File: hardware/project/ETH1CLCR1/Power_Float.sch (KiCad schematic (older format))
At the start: 56 parts, among them U602 LM1117IMP-3.3/NOPB, U604 LM1117IMP-3.3/NOPB, U608 LM1117IMP-5.0/NOPB, U609 TSR1-2490, U701 THL15-2415WI, U703 MC7815BD2TG, U705 TSR2-2450, U706 LT8330_S6, U707 MC7915BD2TG, U710 LT8330_S6

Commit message: Schematic design
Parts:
- removed U703: MC7815BD2TG, Package_TO_SOT_SMD:TO-263-2, symbol Regulator_Linear:L7815
- removed U707: MC7915BD2TG, Package_TO_SOT_SMD:TO-263-2, symbol Regulator_Linear:L7915
- added U?: L7815, symbol Regulator_Linear:L7815
- added U?: L7915, symbol Regulator_Linear:L7915
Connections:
- net +15VF: now also U?.3 (OUT)
- net -15VF: now also U?.3 (VO)
- net AGNDF: now also U?.1 (GND), U?.2 (GND)
- net at C715.1, C716.1, C717.1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: now also U?.1 (IN)
- net at C726.1, C727.1, C728.1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: now also U?.2 (VI)
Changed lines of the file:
@@
 $Descr A4 11693 8268
 encoding utf-8
-Sheet 8 13
+Sheet 6 14
 Title ""
 Date ""
@@
 	650  3100 650  3250
 Connection ~ 650  3250
-$Comp
-L Regulator_Linear:L7815 U703
-U 1 1 5DD99E27
-P 5400 3250
-F 0 "U703" H 5400 3492 50  0000 C CNN
-F 1 "MC7815BD2TG" H 5400 3401 50  0000 C CNN
-F 2 "Package_TO_SOT_SMD:TO-263-2" H 5425 3100 50  0001 L CIN
-F 3 "http://www.st.com/content/ccc/resource/technical/document/datasheet/41/4f/b3/b0/12/d4/47/88/CD00000444.pdf/files/CD00000444.pdf/jcr:content/translations/en.CD00000444.pdf" H 5400 3200 50  0001 C CNN
-	1    5400 3250
-	1    0    0    -1
-$EndComp
 Wire Wire Line
 	5100 3250 4900 3250
@@
 	3450 6850 4300 6850
 Connection ~ 3450 6850
-$Comp
-L Regulator_Linear:L7915 U707
-U 1 1 5DE83B07
-P 5400 5400
-F 0 "U707" H 5400 5158 50  0000 C CNN
-F 1 "MC7915BD2TG" H 5400 5249 50  0000 C CNN
-F 2 "Package_TO_SOT_SMD:TO-263-2" H 5400 5200 50  0001 C CIN
-F 3 "http://www.st.com/content/ccc/resource/technical/document/datasheet/c9/16/86/41/c7/2b/45/f2/CD00000450.pdf/files/CD00000450.pdf/jcr:content/translations/en.CD00000450.pdf" H 5400 5400 50  0001 C CNN
-	1    5400 5400
-	1    0    0    1
-$EndComp
 Wire Wire Line
 	10500 5400 10700 5400
@@
 Wire Wire Line
 	5750 5400 5950 5400
+$Comp
+L Regulator_Linear:L7815 U?
+U 1 1 5E3D3561
+P 5400 3250
+F 0 "U?" H 5400 3492 50  0000 C CNN
+F 1 "L7815" H 5400 3401 50  0000 C CNN
+F 2 "" H 5425 3100 50  0001 L CIN
+F 3 "http://www.st.com/content/ccc/resource/technical/document/datasheet/41/4f/b3/b0/12/d4/47/88/CD00000444.pdf/files/CD00000444.pdf/jcr:content/translations/en.CD00000444.pdf" H 5400 3200 50  0001 C CNN
+	1    5400 3250
+	1    0    0    -1
+$EndComp
+$Comp
+L Regulator_Linear:L7915 U?
+U 1 1 5E3D6FD5
+P 5400 5400
+F 0 "U?" H 5400 5158 50  0000 C CNN
+F 1 "L7915" H 5400 5249 50  0000 C CNN
+F 2 "" H 5400 5200 50  0001 C CIN
+F 3 "http://www.st.com/content/ccc/resource/technical/document/datasheet/c9/16/86/41/c7/2b/45/f2/CD00000450.pdf/files/CD00000450.pdf/jcr:content/translations/en.CD00000450.pdf" H 5400 5400 50  0001 C CNN
+	1    5400 5400
+	1    0    0    1
+$EndComp
 $EndSCHEMATC

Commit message: Schematic design
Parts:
- added C? (x2): 4u7/50V, Capacitor_SMD:C_1206_3216Metric_Pad1.42x1.75mm_HandSolder, symbol Device:C
- added U?: L7812, symbol Regulator_Linear:L7815
- added U?: L7912, symbol Regulator_Linear:L7915
- gave numbers to parts that had none: 2
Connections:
- net AGNDF: now also C?.2, C?.2, U?.1 (GND), U?.2 (GND)
- net at C715.1, C716.1, C717.1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: now also U?.1 (IN)
- net at C726.1, C727.1, C728.1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: now also U?.2 (VI)
- new net +12VF: C?.1, U?.3 (OUT)
- new net -12VF: C?.1, U?.3 (VO)
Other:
- moved on the sheet: C701, C702, C703, C704, C705, C706, C707, C708, C709, C710, C711, C712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

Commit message: Schematic design
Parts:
- gave numbers to parts that had none: 4
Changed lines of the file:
@@
 $Descr A4 11693 8268
 encoding utf-8
-Sheet 6 14
+Sheet 6 16
 Title ""
 Date ""
@@
 $EndComp
 $Comp
-L Regulator_Linear:L7815 U?
+L Regulator_Linear:L7815 U606
 U 1 1 5E3BDF7C
 P 5400 1200
-F 0 "U?" H 5400 1442 50  0000 C CNN
+F 0 "U606" H 5400 1442 50  0000 C CNN
 F 1 "L7812" H 5400 1351 50  0000 C CNN
 F 2 "" H 5425 1050 50  0001 L CIN
@@
 	4300 2050 4300 2100
 $Comp
-L ETH1CLCR1:DGNDF #PWR?
+L ETH1CLCR1:DGNDF #PWR0610
 U 1 1 5E3EA298
 P 5400 1550
-F 0 "#PWR?" H 5400 1300 50  0001 C CNN
+F 0 "#PWR0610" H 5400 1300 50  0001 C CNN
 F 1 "DGNDF" H 5405 1377 50  0000 C CNN
 F 2 "" H 5400 1550 50  0001 C CNN
@@
 	5700 1200 5750 1200
 $Comp
-L ETH1CLCR1:+12VF #PWR?
+L ETH1CLCR1:+12VF #PWR0614
 U 1 1 5E414385
 P 5950 1150
-F 0 "#PWR?" H 5950 1000 50  0001 C CNN
+F 0 "#PWR0614" H 5950 1000 50  0001 C CNN
 F 1 "+12VF" H 5965 1323 50  0000 C CNN
 F 2 "" H 5950 1150 50  0001 C CNN
@@
 	4900 1200 4900 2100
 $Comp
-L Regulator_Linear:L7915 U?
+L Regulator_Linear:L7915 U607
 U 1 1 5E495423
 P 5400 4500
-F 0 "U?" H 5400 4258 50  0000 C CNN
+F 0 "U607" H 5400 4258 50  0000 C CNN
 F 1 "L7912" H 5400 4349 50  0000 C CNN
 F 2 "" H 5400 4300 50  0001 C CIN
@@
 $EndComp
 $Comp
-L ETH1CLCR1:DGNDF #PWR?
+L ETH1CLCR1:DGNDF #PWR0611
 U 1 1 5E4A6F1D
 P 5400 4850
-F 0 "#PWR?" H 5400 4600 50  0001 C CNN
+F 0 "#PWR0611" H 5400 4600 50  0001 C CNN
 F 1 "DGNDF" H 5405 4677 50  0000 C CNN
 F 2 "" H 5400 4850 50  0001 C CNN
@@
 	5700 4500 5750 4500
 $Comp
-L ETH1CLCR1:-12VF #PWR?
+L ETH1CLCR1:-12VF #PWR0615
 U 1 1 5E4EFBD2
 P 5950 4450
-F 0 "#PWR?" H 5950 4300 50  0001 C CNN
+F 0 "#PWR0615" H 5950 4300 50  0001 C CNN
 F 1 "-12VF" H 5965 4623 50  0000 C CNN
 F 2 "" H 5950 4450 50  0001 C CNN
@@
 $EndComp
 $Comp
-L Device:C C?
+L Device:C C605
 U 1 1 5E4F3F19
 P 5750 1400
-F 0 "C?" H 5865 1446 50  0000 L CNN
+F 0 "C605" H 5865 1446 50  0000 L CNN
 F 1 "4u7/50V" H 5865 1355 50  0000 L CNN
 F 2 "Capacitor_SMD:C_1206_3216Metric_Pad1.42x1.75mm_HandSolder" H 5788 1250 50  0001 C CNN
@@
 $EndComp
 $Comp
-L ETH1CLCR1:DGNDF #PWR?
+L ETH1CLCR1:DGNDF #PWR0612
 U 1 1 5E4F46AC
 P 5750 1550
-F 0 "#PWR?" H 5750 1300 50  0001 C CNN
+F 0 "#PWR0612" H 5750 1300 50  0001 C CNN
 F 1 "DGNDF" H 5755 1377 50  0000 C CNN
 F 2 "" H 5750 1550 50  0001 C CNN
@@
 	5750 1200 5950 1200
 $Comp
-L Device:C C?
+L Device:C C606
 U 1 1 5E53289B
 P 5750 4700
-F 0 "C?" H 5865 4746 50  0000 L CNN
+F 0 "C606" H 5865 4746 50  0000 L CNN
 F 1 "4u7/50V" H 5865 4655 50  0000 L CNN
 F 2 "Capacitor_SMD:C_1206_3216Metric_Pad1.42x1.75mm_HandSolder" H 5788 4550 50  0001 C CNN
@@
 $EndComp
 $Comp
-L ETH1CLCR1:DGNDF #PWR?
+L ETH1CLCR1:DGNDF #PWR0613
 U 1 1 5E5328A1
 P 5750 4850
-F 0 "#PWR?" H 5750 4600 50  0001 C CNN
+F 0 "#PWR0613" H 5750 4600 50  0001 C CNN
 F 1 "DGNDF" H 5755 4677 50  0000 C CNN
 F 2 "" H 5750 4850 50  0001 C CNN

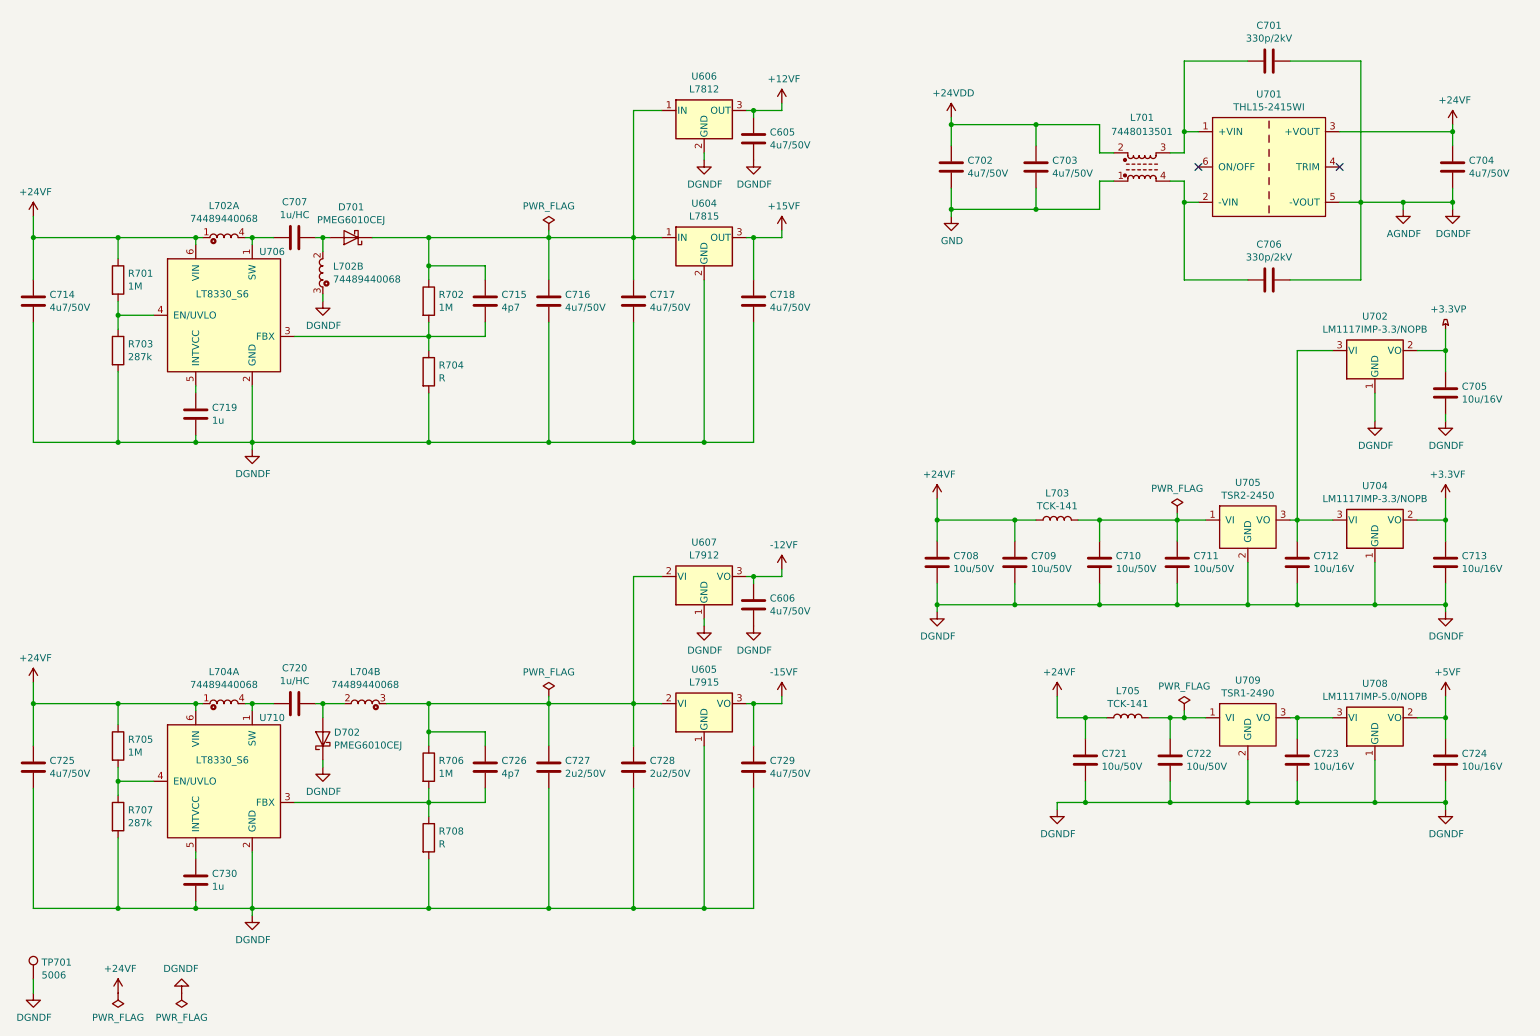
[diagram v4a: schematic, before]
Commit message: Footprint asigment (not finished).
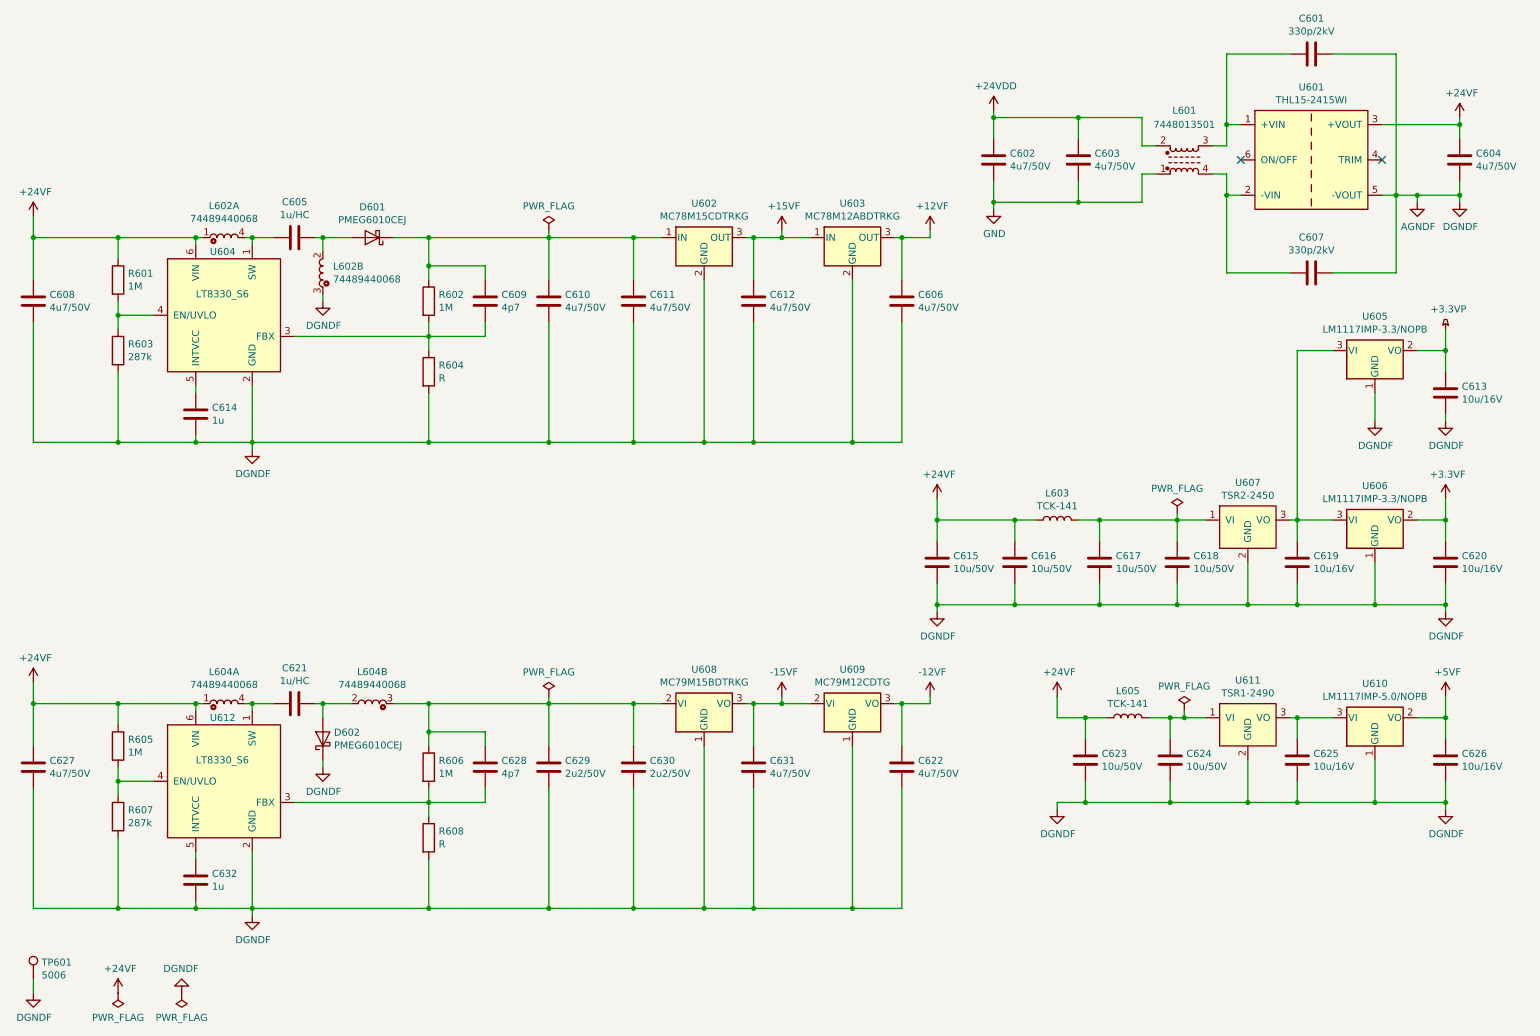
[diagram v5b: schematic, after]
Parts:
- removed U605: L7915, symbol Regulator_Linear:L7915
- removed U607: L7912, symbol Regulator_Linear:L7915
- added U608: MC79M15BDTRKG, Package_TO_SOT_SMD:TO-252-2, symbol Regulator_Linear:MC79M15_TO252
- added U609: MC79M12CDTG, Package_TO_SOT_SMD:TO-252-2, symbol Regulator_Linear:MC79M12_TO252
- C614: renamed from C719; footprint Capacitor_SMD:C_0603_1608Metric_Pad1.05x0.95mm_HandSolder -> Capacitor_SMD:C_0805_2012Metric_Pad1.15x1.40mm_HandSolder
- C632: renamed from C730; footprint Capacitor_SMD:C_0603_1608Metric_Pad1.05x0.95mm_HandSolder -> Capacitor_SMD:C_0805_2012Metric_Pad1.15x1.40mm_HandSolder
- U602: renamed from U604; value L7815 -> MC78M15CDTRKG; footprint (none) -> Package_TO_SOT_SMD:TO-252-2
- U603: renamed from U606; value L7812 -> MC78M12ABDTRKG; footprint (none) -> Package_TO_SOT_SMD:TO-252-2
- renumbered C707 to C605, C605 to C606, C606 to C607, C714 to C608, C715 to C609, C716 to C610, C717 to C611, C718 to C612, C605 to C613, C608 to C615, C609 to C616, C610 to C617, C611 to C618, C612 to C619, C613 to C620, C720 to C621, C606 to C622, C621 to C623, C622 to C624, C623 to C625, C624 to C626, C725 to C627, C726 to C628, C727 to C629, C728 to C630, C729 to C631, D701 to D601, D702 to D602, L701 to L601, L702 to L602, L704 to L604, R701 to R601, R702 to R602, R703 to R603, R704 to R604, R705 to R605, R706 to R606, R707 to R607, R708 to R608, U701 to U601, U706 to U604, U602 to U605, U604 to U606, U705 to U607, U608 to U610, U609 to U611, U710 to U612
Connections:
- net +15VF: now also U603.1 (IN)
- net -12VF: now also U609.3 (VO)
- net -15VF: now also U608.3 (VO), U609.2 (VI)
- net AGNDF: now also U608.1 (GND), U609.1 (GND)
- net at C609.1, C610.1, C611.1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: no longer U603.1 (IN)
- net at C628.1, C629.1, C630.1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: now also U608.2 (VI)
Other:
- moved on the sheet: C601, C602, C603, C604, C606, C607, C622, D601, L601, L604B, U601, U603

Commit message: Modification in schematic and PCB layout.
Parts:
- C614, C632: footprint Capacitor_SMD:C_0805_2012Metric_Pad1.15x1.40mm_HandSolder -> Capacitor_SMD:C_0603_1608Metric_Pad1.05x0.95mm_HandSolder
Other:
- moved on the sheet: C601, C602, C603, C604, C605, C606, C607, C609, C610, C611, C612, C614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

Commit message: PCB layout
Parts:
- U602: value MC78M15CDTRKG -> MC7815BD2TG; footprint Package_TO_SOT_SMD:TO-252-2 -> Package_TO_SOT_SMD:TO-263-2
- U608: value MC79M15BDTRKG -> MC7915BD2TG; footprint Package_TO_SOT_SMD:TO-252-2 -> Package_TO_SOT_SMD:TO-263-2
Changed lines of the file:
@@
 P 5300 2100
 F 0 "U602" H 5300 2342 50  0000 C CNN
-F 1 "MC78M15CDTRKG" H 5300 2251 50  0000 C CNN
-F 2 "Package_TO_SOT_SMD:TO-252-2" H 5325 1950 50  0001 L CIN
+F 1 "MC7815BD2TG " H 5300 2251 50  0000 C CNN
+F 2 "Package_TO_SOT_SMD:TO-263-2" H 5325 1950 50  0001 L CIN
 F 3 "http://www.st.com/content/ccc/resource/technical/document/datasheet/41/4f/b3/b0/12/d4/47/88/CD00000444.pdf/files/CD00000444.pdf/jcr:content/translations/en.CD00000444.pdf" H 5300 2050 50  0001 C CNN
 	1    5300 2100
@@
 P 5300 5400
 F 0 "U608" H 5300 5158 50  0000 C CNN
-F 1 "MC79M15BDTRKG" H 5300 5249 50  0000 C CNN
-F 2 "Package_TO_SOT_SMD:TO-252-2" H 5300 5200 50  0001 C CIN
+F 1 "MC7915BD2TG" H 5300 5249 50  0000 C CNN
+F 2 "Package_TO_SOT_SMD:TO-263-2" H 5300 5200 50  0001 C CIN
 F 3 "http://www.onsemi.com/pub/Collateral/MC79M00-D.PDF" H 5300 5400 50  0001 C CNN
 	1    5300 5400

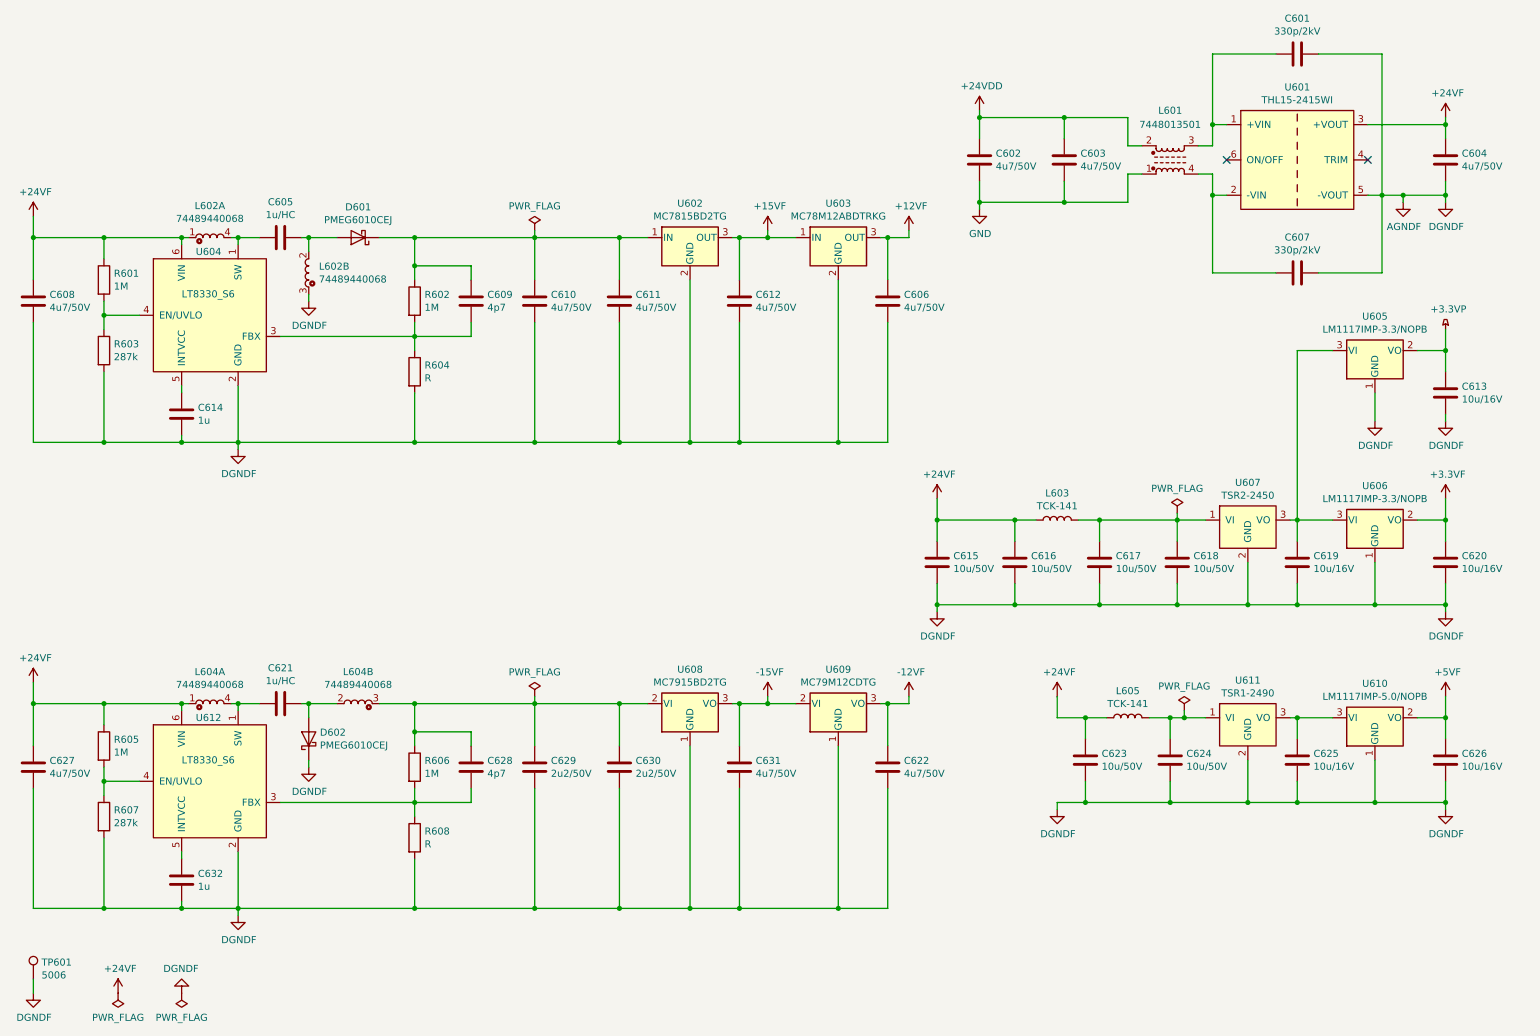
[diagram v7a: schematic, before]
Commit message: Redesinged ADC schematic.
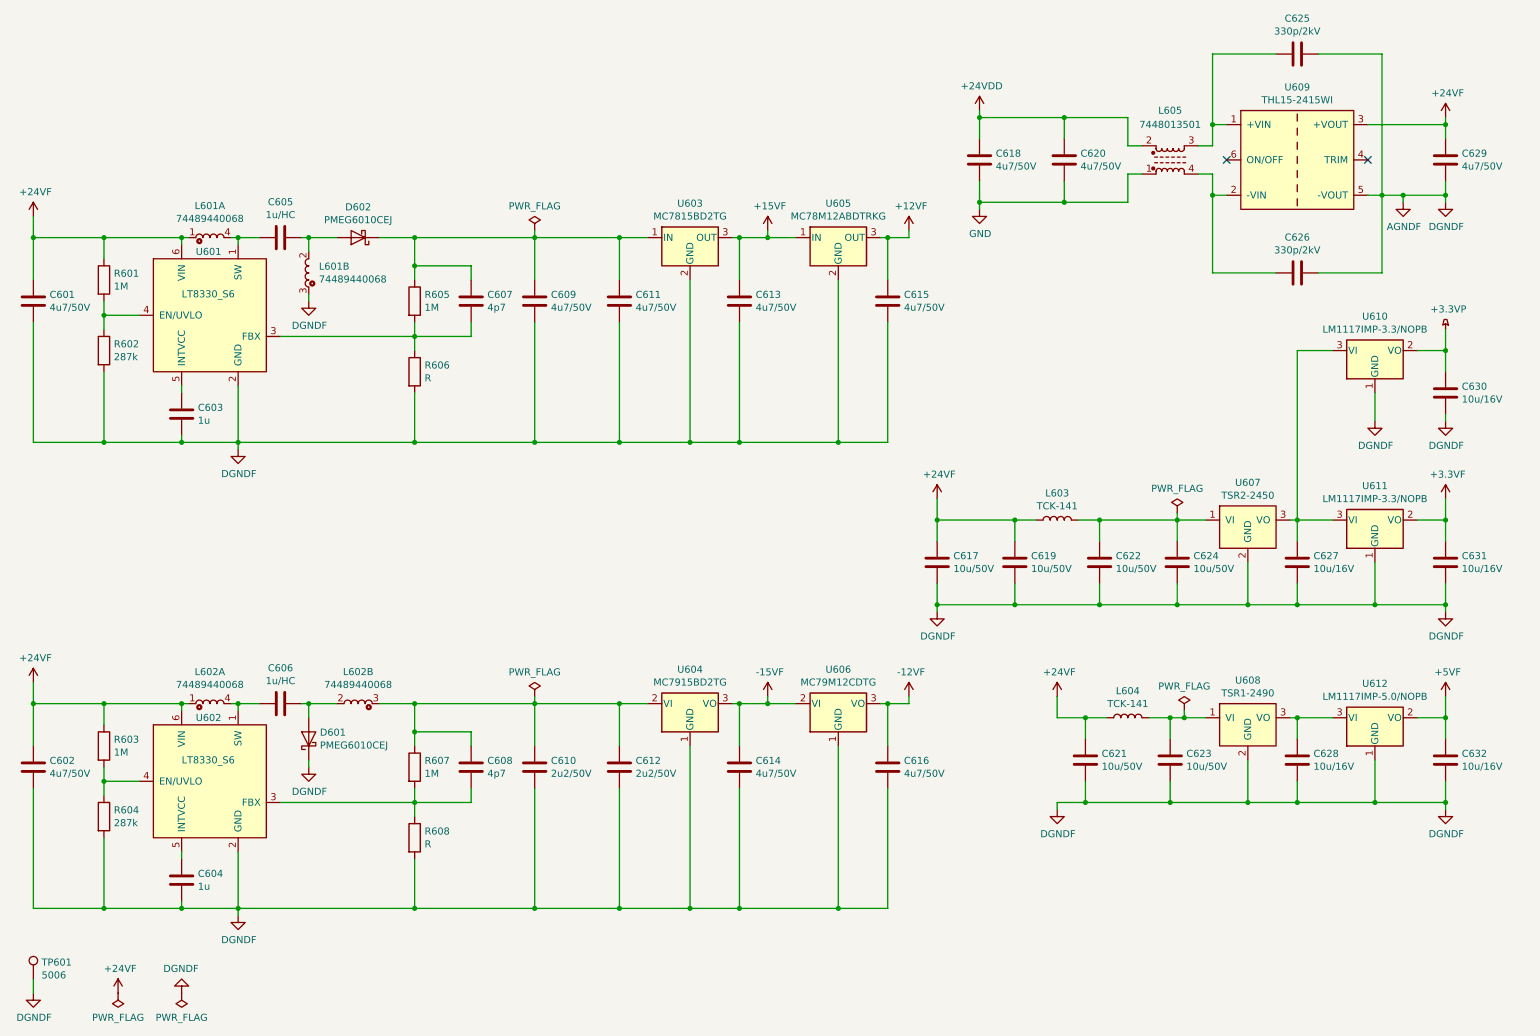
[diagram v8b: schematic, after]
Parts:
- renumbered C608 to C601, C627 to C602, C614 to C603, C632 to C604, C621 to C606, C609 to C607, C628 to C608, C610 to C609, C629 to C610, C630 to C612, C612 to C613, C631 to C614, C606 to C615, C622 to C616, C615 to C617, C602 to C618, C616 to C619, C603 to C620, C623 to C621, C617 to C622, C624 to C623, C618 to C624, C601 to C625, C607 to C626, C619 to C627, C625 to C628, C604 to C629, C613 to C630, C620 to C631, C626 to C632, D602 to D601, D601 to D602, L602 to L601, L604 to L602, L605 to L604, L601 to L605, R603 to R602, R605 to R603, R607 to R604, R602 to R605, R604 to R606, R606 to R607, U604 to U601, U612 to U602, U602 to U603, U608 to U604, U603 to U605, U609 to U606, U611 to U608, U601 to U609, U605 to U610, U606 to U611, U610 to U612
